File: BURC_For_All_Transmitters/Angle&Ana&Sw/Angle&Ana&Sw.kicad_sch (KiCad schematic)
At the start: 23 parts, among them J1 Conn_01x04, J10 Conn_ButtonsRight, J10B1 Conn_ButtonsRight, J2 I2C_INPUT, J3 I2C_INPUT, J4 I2C_INPUT, J5 I2C_INPUT, J6 Conn_ToButtonsLeft, J7 Conn_FromButtonsLeft, J9 Conn_ButtonsLeft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

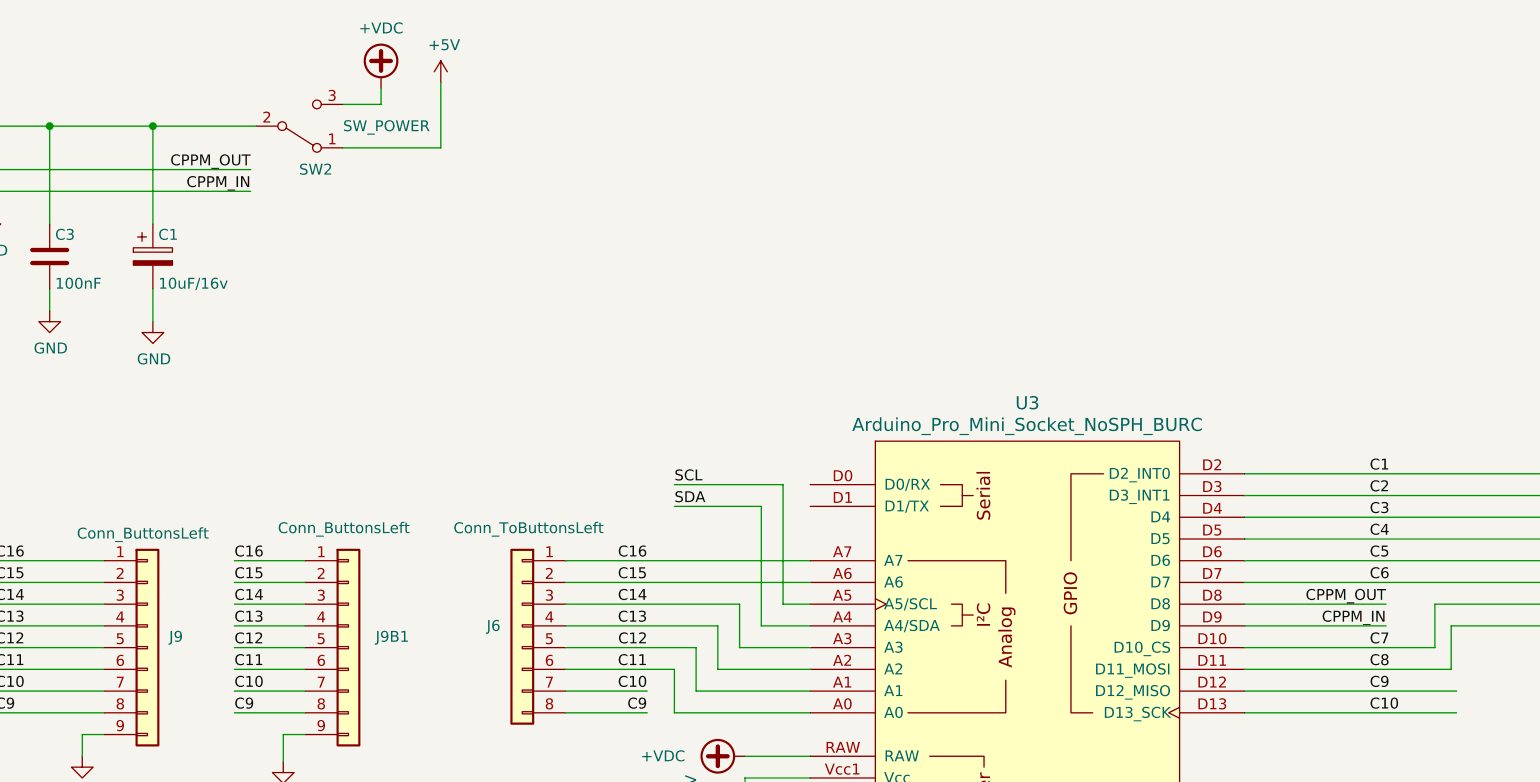
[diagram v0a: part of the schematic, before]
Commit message: Swap CPPM_IN/CPPM_OUT
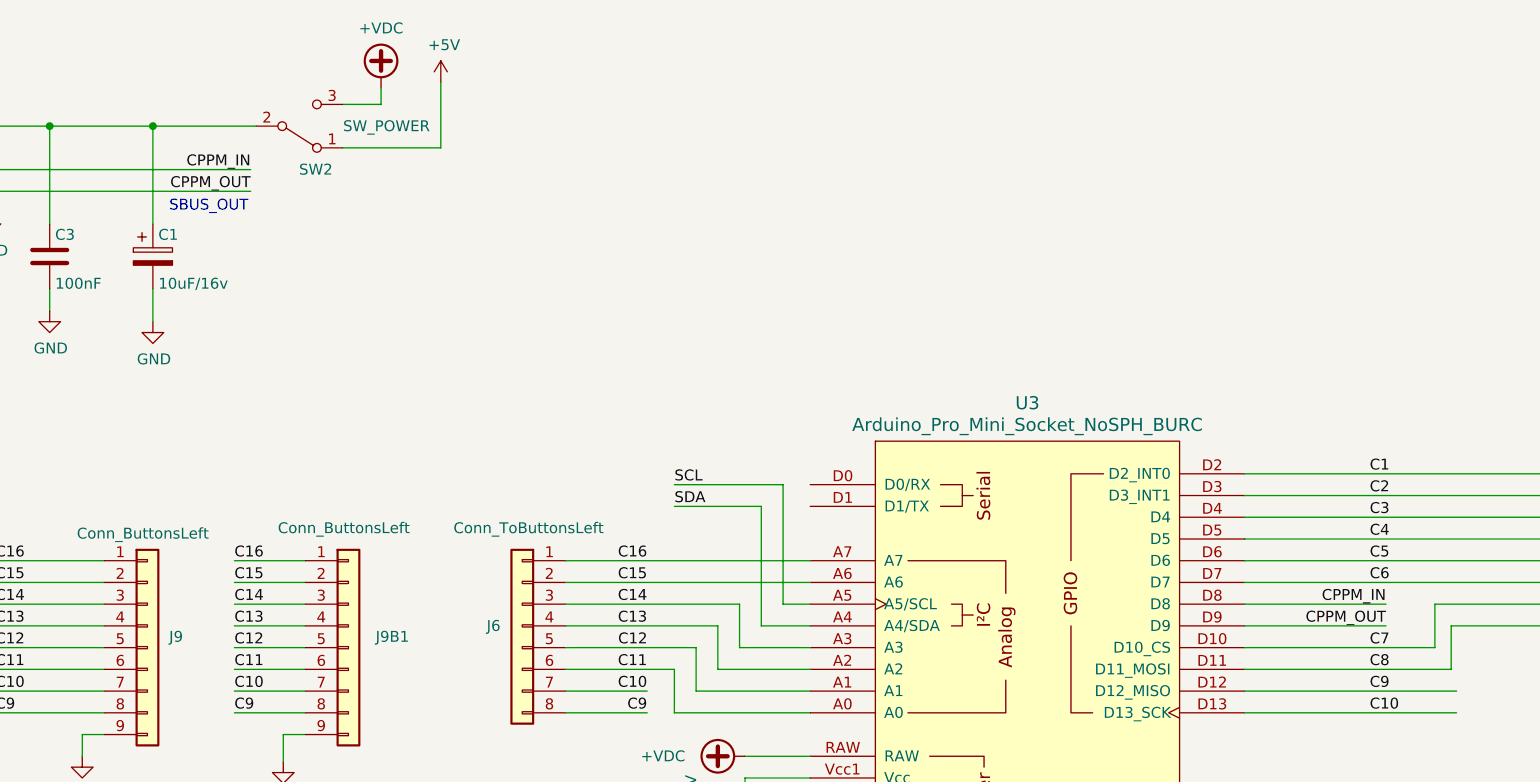
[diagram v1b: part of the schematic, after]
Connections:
- net CPPM_IN: now also J1.2 (Pin_2), U3.D8; no longer J1.1 (Pin_1), U3.D9
- net CPPM_OUT: now also J1.1 (Pin_1), U3.D9; no longer J1.2 (Pin_2), U3.D8
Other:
- note added: "SBUS_OUT"
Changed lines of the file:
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@@
   (title_block
     (title "Board for Angle & Ana & Sw")
-    (date "2023-08-31")
+    (date "2023-09-10")
     (rev "1.0")
     (company "OpenAVRc")
@@
     (stroke (width 0) (type default))
   )
+  (text "SBUS_OUT" (at 58.42 45.72 0)
+    (effects (font (size 1.27 1.27)) (justify left bottom))
+  )
   (label "C10" (at 198.755 104.14 0) (fields_autoplaced)
     (effects (font (size 1.27 1.27)) (justify left bottom))
@@
     (effects (font (size 1.27 1.27)) (justify left bottom))
   )
-  (label "CPPM_OUT" (at 67.945 40.64 180) (fields_autoplaced)
+  (label "CPPM_OUT" (at 67.945 43.18 180) (fields_autoplaced)
     (effects (font (size 1.27 1.27)) (justify right bottom))
   )
@@
     (effects (font (size 1.27 1.27)) (justify left bottom))
   )
-  (label "CPPM_IN" (at 200.66 93.98 180) (fields_autoplaced)
+  (label "CPPM_IN" (at 200.66 91.44 180) (fields_autoplaced)
     (effects (font (size 1.27 1.27)) (justify right bottom))
   )
@@
     (effects (font (size 1.27 1.27)) (justify left bottom))
   )
-  (label "CPPM_OUT" (at 200.66 91.44 180) (fields_autoplaced)
+  (label "CPPM_OUT" (at 200.66 93.98 180) (fields_autoplaced)
     (effects (font (size 1.27 1.27)) (justify right bottom))
   )
@@
     (effects (font (size 1.27 1.27)) (justify left bottom))
   )
-  (label "CPPM_IN" (at 67.945 43.18 180) (fields_autoplaced)
-    (effects (font (size 1.27 1.27)) (justify right bottom))
-  )
+  (label "CPPM_IN" (at 67.945 40.64 180) (fields_autoplaced)
+    (effects (font (size 1.27 1.27)) (justify right bottom))
+  )
